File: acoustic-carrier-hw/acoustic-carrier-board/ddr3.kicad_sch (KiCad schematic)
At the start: 21 parts, among them IC2 MT41K256M16TW-107_P

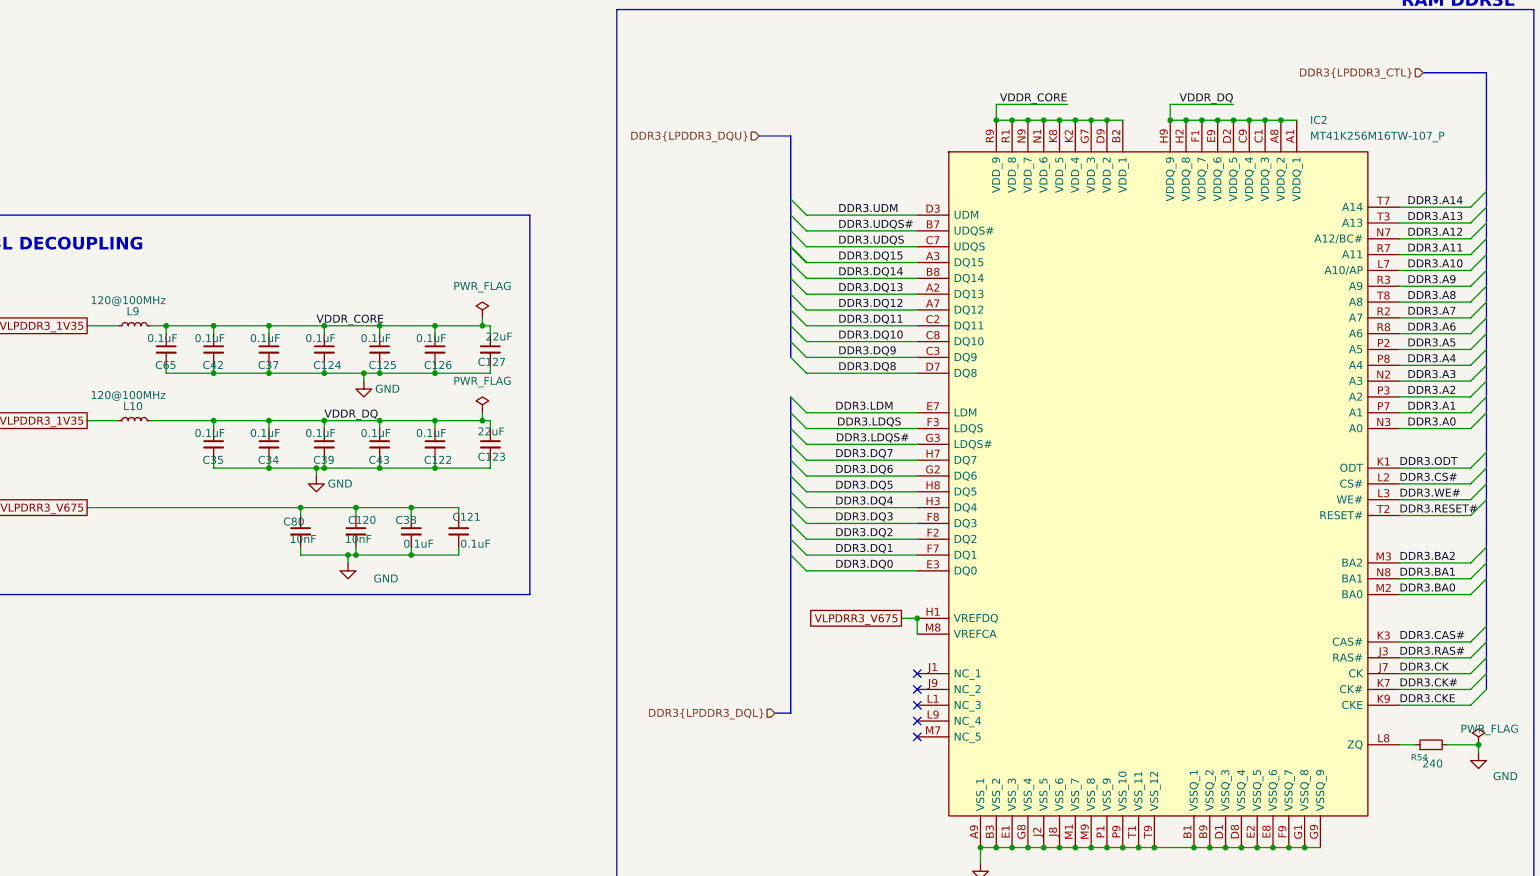
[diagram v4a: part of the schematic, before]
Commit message: [carrier] Finished rough layout, p (put together according to component category
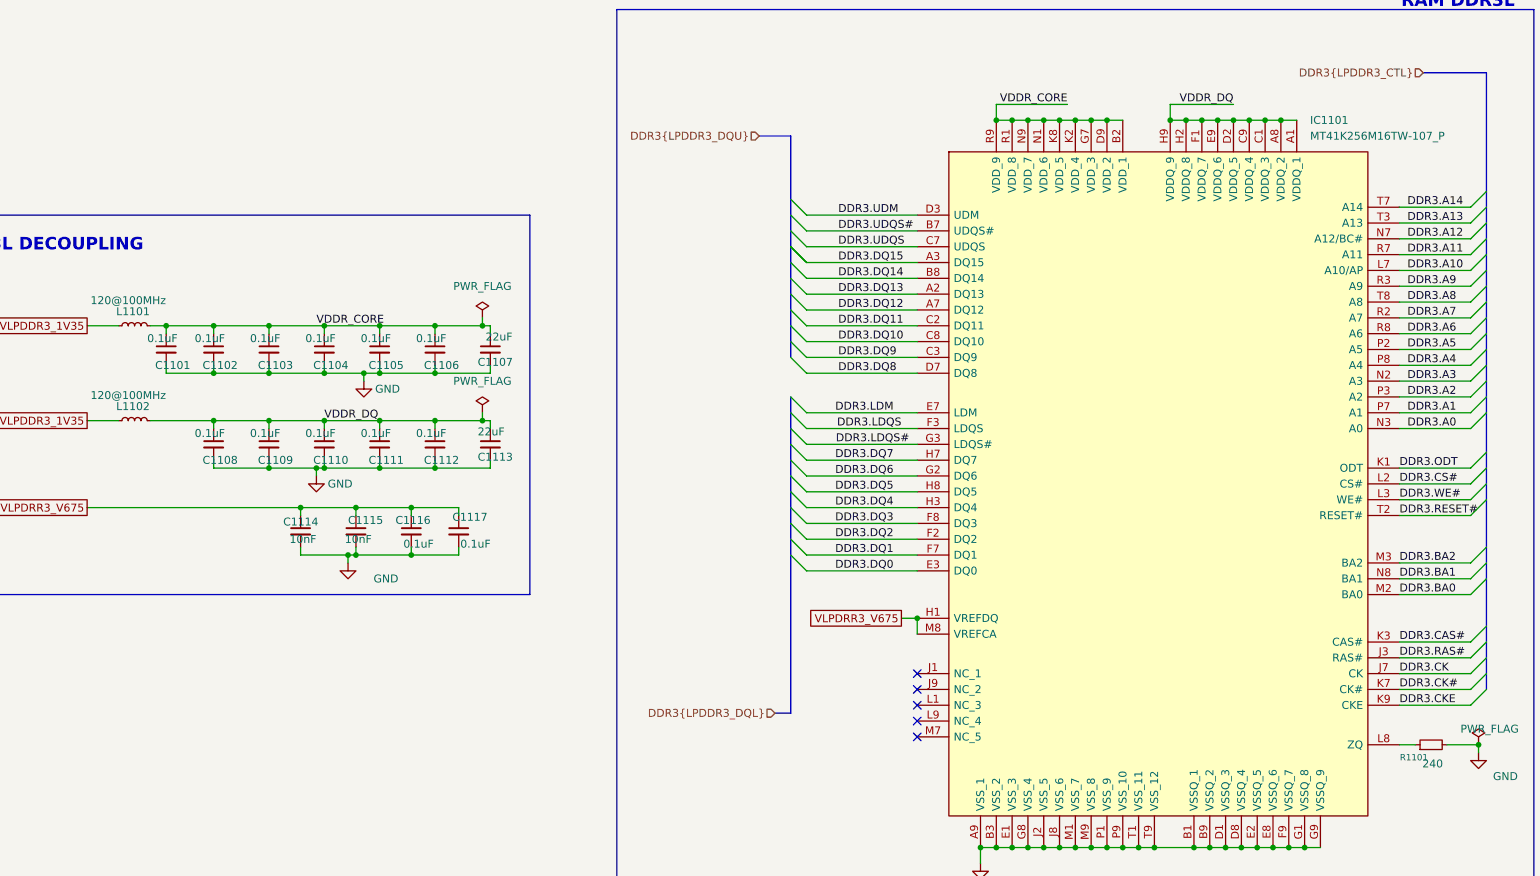
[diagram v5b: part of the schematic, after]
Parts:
- renumbered C65 to C1101, C42 to C1102, C37 to C1103, C124 to C1104, C125 to C1105, C126 to C1106, C127 to C1107, C35 to C1108, C34 to C1109, C39 to C1110, C43 to C1111, C122 to C1112, C123 to C1113, C80 to C1114, C120 to C1115, C38 to C1116, C121 to C1117, IC2 to IC1101, L9 to L1101, L10 to L1102, R54 to R1101
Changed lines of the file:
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@@
 		(on_board yes)
 		(dnp no)
-		(property "Reference" "C42"
+		(property "Reference" "C1102"
 			(at 69.342 74.93 0)
 			(effects
@@
 			(project "acoustic-carrier-board"
 				(path "/25b015c9-ab13-4427-b72c-b6f348597100/f2b9f5c5-2b83-49a1-9584-962bb926f77f"
-					(reference "C42")
+					(reference "C1102")
 					(unit 1)
 				)
@@
 		(on_board yes)
 		(dnp no)
-		(property "Reference" "C34"
+		(property "Reference" "C1109"
 			(at 78.232 90.17 0)
 			(effects
@@
 			(project "acoustic-carrier-board"
 				(path "/25b015c9-ab13-4427-b72c-b6f348597100/f2b9f5c5-2b83-49a1-9584-962bb926f77f"
-					(reference "C34")
+					(reference "C1109")
 					(unit 1)
 				)
@@
 		(on_board yes)
 		(dnp no)
-		(property "Reference" "#PWR01"
+		(property "Reference" "#PWR01104"
 			(at 274.32 143.51 0)
 			(effects
@@
 			(project "acoustic-carrier-board"
 				(path "/25b015c9-ab13-4427-b72c-b6f348597100/f2b9f5c5-2b83-49a1-9584-962bb926f77f"
-					(reference "#PWR01")
+					(reference "#PWR01104")
 					(unit 1)
 				)
@@
 		(on_board yes)
 		(dnp no)
-		(property "Reference" "C39"
+		(property "Reference" "C1110"
 			(at 87.122 90.17 0)
 			(effects
@@
 			(project "acoustic-carrier-board"
 				(path "/25b015c9-ab13-4427-b72c-b6f348597100/f2b9f5c5-2b83-49a1-9584-962bb926f77f"
-					(reference "C39")
+					(reference "C1110")
 					(unit 1)
 				)
@@
 		(on_board yes)
 		(dnp no)
-		(property "Reference" "#PWR04"
+		(property "Reference" "#PWR01102"
 			(at 87.63 99.06 0)
 			(effects
@@
 			(project "acoustic-carrier-board"
 				(path "/25b015c9-ab13-4427-b72c-b6f348597100/f2b9f5c5-2b83-49a1-9584-962bb926f77f"
-					(reference "#PWR04")
+					(reference "#PWR01102")
 					(unit 1)
 				)
@@
 		(on_board yes)
 		(dnp no)
-		(property "Reference" "C122"
+		(property "Reference" "C1112"
 			(at 104.902 90.17 0)
 			(effects
@@
 			(project "acoustic-carrier-board"
 				(path "/25b015c9-ab13-4427-b72c-b6f348597100/f2b9f5c5-2b83-49a1-9584-962bb926f77f"
-					(reference "C122")
+					(reference "C1112")
 					(unit 1)
 				)
@@
 		(on_board yes)
 		(dnp no)
-		(property "Reference" "#PWR079"
+		(property "Reference" "#PWR01101"
 			(at 95.25 83.82 0)
 			(effects
@@
 			(project "acoustic-carrier-board"
 				(path "/25b015c9-ab13-4427-b72c-b6f348597100/f2b9f5c5-2b83-49a1-9584-962bb926f77f"
-					(reference "#PWR079")
+					(reference "#PWR01101")
 					(unit 1)
 				)
@@
 		(on_board yes)
 		(dnp no)
-		(property "Reference" "L10"
+		(property "Reference" "L1102"
 			(at 58.166 81.534 90)
 			(effects
@@
 			(project "acoustic-carrier-board"
 				(path "/25b015c9-ab13-4427-b72c-b6f348597100/f2b9f5c5-2b83-49a1-9584-962bb926f77f"
-					(reference "L10")
+					(reference "L1102")
 					(unit 1)
 				)
@@
 		(on_board yes)
 		(dnp no)
-		(property "Reference" "#PWR03"
+		(property "Reference" "#PWR01103"
 			(at 92.71 113.03 0)
 			(effects
@@
 			(project "acoustic-carrier-board"
 				(path "/25b015c9-ab13-4427-b72c-b6f348597100/f2b9f5c5-2b83-49a1-9584-962bb926f77f"
-					(reference "#PWR03")
+					(reference "#PWR01103")
 					(unit 1)
 				)
@@
 		(on_board yes)
 		(dnp no)
-		(property "Reference" "C35"
+		(property "Reference" "C1108"
 			(at 69.342 90.17 0)
 			(effects
@@
 			(project "acoustic-carrier-board"
 				(path "/25b015c9-ab13-4427-b72c-b6f348597100/f2b9f5c5-2b83-49a1-9584-962bb926f77f"
-					(reference "C35")
+					(reference "C1108")
 					(unit 1)
 				)
@@
 		(on_board yes)
 		(dnp no)
-		(property "Reference" "C124"
+		(property "Reference" "C1104"
 			(at 87.122 74.93 0)
 			(effects
@@
 			(project "acoustic-carrier-board"
 				(path "/25b015c9-ab13-4427-b72c-b6f348597100/f2b9f5c5-2b83-49a1-9584-962bb926f77f"
-					(reference "C124")
+					(reference "C1104")
 					(unit 1)
 				)
@@
 		(on_board yes)
 		(dnp no)
-		(property "Reference" "L9"
+		(property "Reference" "L1101"
 			(at 58.166 66.294 90)
 			(effects
@@
 			(project "acoustic-carrier-board"
 				(path "/25b015c9-ab13-4427-b72c-b6f348597100/f2b9f5c5-2b83-49a1-9584-962bb926f77f"
-					(reference "L9")
+					(reference "L1101")
 					(unit 1)
 				)
@@
 		(on_board yes)
 		(dnp no)
-		(property "Reference" "C120"
+		(property "Reference" "C1115"
 			(at 92.71 99.822 0)
 			(effects
@@
 			(project "acoustic-carrier-board"
 				(path "/25b015c9-ab13-4427-b72c-b6f348597100/f2b9f5c5-2b83-49a1-9584-962bb926f77f"
-					(reference "C120")
+					(reference "C1115")
 					(unit 1)
 				)
@@
 		(dnp no)
 		(fields_autoplaced yes)
-		(property "Reference" "#FLG03"
+		(property "Reference" "#FLG01101"
 			(at 114.3 65.405 0)
 			(effects
@@
 			(project "acoustic-carrier-board"
 				(path "/25b015c9-ab13-4427-b72c-b6f348597100/f2b9f5c5-2b83-49a1-9584-962bb926f77f"
-					(reference "#FLG03")
+					(reference "#FLG01101")
 					(unit 1)
 				)
@@
 		(on_board yes)
 		(dnp no)
-		(property "Reference" "C43"
+		(property "Reference" "C1111"
 			(at 96.012 90.17 0)
 			(effects
@@
 			(project "acoustic-carrier-board"
 				(path "/25b015c9-ab13-4427-b72c-b6f348597100/f2b9f5c5-2b83-49a1-9584-962bb926f77f"
-					(reference "C43")
+					(reference "C1111")
 					(unit 1)
 				)
@@
 		(on_board yes)
 		(dnp no)
-		(property "Reference" "C121"
+		(property "Reference" "C1117"
 			(at 109.474 99.314 0)
 			(effects
@@
 			(project "acoustic-carrier-board"
 				(path "/25b015c9-ab13-4427-b72c-b6f348597100/f2b9f5c5-2b83-49a1-9584-962bb926f77f"
-					(reference "C121")
+					(reference "C1117")
 					(unit 1)
 				)
@@
 		(on_board yes)
 		(dnp no)
-		(property "Reference" "C125"
+		(property "Reference" "C1105"
 			(at 96.012 74.93 0)
 			(effects
@@
 			(project "acoustic-carrier-board"
 				(path "/25b015c9-ab13-4427-b72c-b6f348597100/f2b9f5c5-2b83-49a1-9584-962bb926f77f"
-					(reference "C125")
+					(reference "C1105")
 					(unit 1)
 				)
@@
 		(dnp no)
 		(fields_autoplaced yes)
-		(property "Reference" "IC2"
+		(property "Reference" "IC1101"
 			(at 247.2533 35.56 0)
 			(effects
@@
 			(project "acoustic-carrier-board"
 				(path "/25b015c9-ab13-4427-b72c-b6f348597100/f2b9f5c5-2b83-49a1-9584-962bb926f77f"
-					(reference "IC2")
+					(reference "IC1101")
 					(unit 1)
 				)
@@
 		(on_board yes)
 		(dnp no)
-		(property "Reference" "C123"
+		(property "Reference" "C1113"
 			(at 113.538 89.662 0)
 			(effects
@@
 			(project "acoustic-carrier-board"
 				(path "/25b015c9-ab13-4427-b72c-b6f348597100/f2b9f5c5-2b83-49a1-9584-962bb926f77f"
-					(reference "C123")
+					(reference "C1113")
 					(unit 1)
 				)
@@
 		(on_board yes)
 		(dnp no)
-		(property "Reference" "C38"
+		(property "Reference" "C1116"
 			(at 100.33 99.822 0)
 			(effects
@@
 			(project "acoustic-carrier-board"
 				(path "/25b015c9-ab13-4427-b72c-b6f348597100/f2b9f5c5-2b83-49a1-9584-962bb926f77f"
-					(reference "C38")
+					(reference "C1116")
 					(unit 1)
 				)
@@
 		(on_board yes)
 		(dnp no)
-		(property "Reference" "C37"
+		(property "Reference" "C1103"
 			(at 78.232 74.93 0)
 			(effects
@@
 			(project "acoustic-carrier-board"
 				(path "/25b015c9-ab13-4427-b72c-b6f348597100/f2b9f5c5-2b83-49a1-9584-962bb926f77f"
-					(reference "C37")
+					(reference "C1103")
 					(unit 1)
 				)
@@
 		(dnp no)
 		(fields_autoplaced yes)
-		(property "Reference" "#FLG015"
+		(property "Reference" "#FLG01102"
 			(at 114.3 80.645 0)
 			(effects
@@
 			(project "acoustic-carrier-board"
 				(path "/25b015c9-ab13-4427-b72c-b6f348597100/f2b9f5c5-2b83-49a1-9584-962bb926f77f"
-					(reference "#FLG015")
+					(reference "#FLG01102")
 					(unit 1)
 				)
@@
 		(on_board yes)
 		(dnp no)
-		(property "Reference" "C80"
+		(property "Reference" "C1114"
 			(at 82.296 100.076 0)
 			(effects
@@
 			(project "acoustic-carrier-board"
 				(path "/25b015c9-ab13-4427-b72c-b6f348597100/f2b9f5c5-2b83-49a1-9584-962bb926f77f"
-					(reference "C80")
+					(reference "C1114")
 					(unit 1)
 				)
@@
 		(on_board yes)
 		(dnp no)
-		(property "Reference" "R54"
+		(property "Reference" "R1101"
 			(at 266.192 137.922 90)
 			(effects
@@
 			(project "acoustic-carrier-board"
 				(path "/25b015c9-ab13-4427-b72c-b6f348597100/f2b9f5c5-2b83-49a1-9584-962bb926f77f"
-					(reference "R54")
+					(reference "R1101")
 					(unit 1)
 				)
@@
 		(on_board yes)
 		(dnp no)
-		(property "Reference" "C126"
+		(property "Reference" "C1106"
 			(at 104.902 74.93 0)
 			(effects
@@
 			(project "acoustic-carrier-board"
 				(path "/25b015c9-ab13-4427-b72c-b6f348597100/f2b9f5c5-2b83-49a1-9584-962bb926f77f"
-					(reference "C126")
+					(reference "C1106")
 					(unit 1)
 				)
@@
 		(on_board yes)
 		(dnp no)
-		(property "Reference" "C127"
+		(property "Reference" "C1107"
 			(at 113.538 74.422 0)
 			(effects
@@
 			(project "acoustic-carrier-board"
 				(path "/25b015c9-ab13-4427-b72c-b6f348597100/f2b9f5c5-2b83-49a1-9584-962bb926f77f"
-					(reference "C127")
+					(reference "C1107")
 					(unit 1)
 				)
@@
 		(on_board yes)
 		(dnp no)
-		(property "Reference" "C65"
+		(property "Reference" "C1101"
 			(at 61.722 74.93 0)
 			(effects
@@
 			(project "acoustic-carrier-board"
 				(path "/25b015c9-ab13-4427-b72c-b6f348597100/f2b9f5c5-2b83-49a1-9584-962bb926f77f"
-					(reference "C65")
+					(reference "C1101")
 					(unit 1)
 				)
@@
 		(on_board yes)
 		(dnp no)
-		(property "Reference" "#PWR010"
+		(property "Reference" "#PWR01105"
 			(at 194.31 161.29 0)
 			(effects
@@
 			(project "acoustic-carrier-board"
 				(path "/25b015c9-ab13-4427-b72c-b6f348597100/f2b9f5c5-2b83-49a1-9584-962bb926f77f"
-					(reference "#PWR010")
+					(reference "#PWR01105")
 					(unit 1)
 				)
@@
 		(on_board yes)
 		(dnp no)
-		(property "Reference" "#FLG018"
+		(property "Reference" "#FLG01103"
 			(at 274.32 133.985 0)
 			(effects
@@
 			(project "acoustic-carrier-board"
 				(path "/25b015c9-ab13-4427-b72c-b6f348597100/f2b9f5c5-2b83-49a1-9584-962bb926f77f"
-					(reference "#FLG018")
+					(reference "#FLG01103")
 					(unit 1)
 				)
